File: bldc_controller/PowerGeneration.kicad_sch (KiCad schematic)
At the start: 67 parts, among them U2 MAX15062BATA+T, U3 ADP5301ACBZ-4-R7, U4 LP2992IM5-3.3/NOPB

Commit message: some progress on the pcb
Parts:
- removed NT2: GND_STAR, NetTie:NetTie-2_SMD_Pad2.0mm, symbol Device:NetTie_2
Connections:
- net +VBAT: no longer C?.2, C?.2, C?.2, C?.2, C?.2, C?.2, C?.2, C?.2, C?.2, C?.2, C?.2, C?.2, C?.2, C?.2, C?.2, C?.2
- net -VBAT: now also C?.2, C?.2, C?.2, C?.2, C?.2, C?.2, C?.2, C?.2, C?.2, C?.2, C?.2, C?.2, C?.2, C?.2, C?.2, C?.2
- net VID_3V3: now reaches U3.C3 (VID)
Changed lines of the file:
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@@
   )
   (no_connect (at 105.41 40.64))
-  (no_connect (at 217.17 45.72))
-  (no_connect (at 240.03 45.72))
+  (no_connect (at 208.28 45.72))
+  (no_connect (at 248.92 45.72))
   (wire (pts (xy 111.76 140.97) (xy 111.76 139.7))
     (stroke (width 0.381) (type default) (color 200 50 50 1))
@@
     (stroke (width 0.381) (type default) (color 0 0 0 1))
   )
+  (wire (pts (xy 248.92 45.72) (xy 240.03 45.72))
+    (stroke (width 0) (type default))
+  )
   (wire (pts (xy 27.94 139.7) (xy 31.75 139.7))
     (stroke (width 0.381) (type default) (color 200 50 50 1))
@@
     (stroke (width 0) (type default))
   )
-  (wire (pts (xy 229.87 142.24) (xy 233.68 142.24))
-    (stroke (width 0) (type default))
-  )
   (wire (pts (xy 217.17 33.02) (xy 215.9 33.02))
     (stroke (width 0) (type default))
@@
     (stroke (width 0) (type default))
   )
+  (wire (pts (xy 208.28 45.72) (xy 217.17 45.72))
+    (stroke (width 0) (type default))
+  )
   (wire (pts (xy 58.42 148.59) (xy 58.42 149.86))
     (stroke (width 0.381) (type default) (color 0 0 0 1))
@@
     (stroke (width 0.381) (type default) (color 0 0 0 1))
   )
-  (polyline (pts (xy 274.32 161.29) (xy 181.61 161.29))
-    (stroke (width 0) (type default))
-  )
   (wire (pts (xy 102.87 154.94) (xy 102.87 156.21))
     (stroke (width 0.381) (type default) (color 200 50 50 1))
@@
     (stroke (width 0.381) (type default) (color 200 50 50 1))
   )
-  (wire (pts (xy 217.17 146.05) (xy 219.71 146.05))
-    (stroke (width 0.381) (type default) (color 0 0 0 1))
-  )
   (wire (pts (xy 255.27 92.71) (xy 238.76 92.71))
     (stroke (width 0) (type default))
@@
     (stroke (width 0.381) (type default) (color 0 0 0 1))
   )
-  (wire (pts (xy 233.68 142.24) (xy 233.68 144.78))
-    (stroke (width 0) (type default))
-  )
   (wire (pts (xy 40.64 154.94) (xy 40.64 156.21))
     (stroke (width 0.381) (type default) (color 200 50 50 1))
@@
     (stroke (width 0) (type default))
   )
-  (polyline (pts (xy 177.8 138.43) (xy 177.8 157.48))
-    (stroke (width 0) (type default))
-  )
   (wire (pts (xy 93.98 170.18) (xy 102.87 170.18))
     (stroke (width 0.381) (type default) (color 200 50 50 1))
@@
     (stroke (width 0.381) (type default) (color 200 50 50 1))
   )
-  (polyline (pts (xy 278.13 138.43) (xy 278.13 157.48))
-    (stroke (width 0) (type default))
-  )
   (wire (pts (xy 35.56 54.61) (xy 30.48 54.61))
     (stroke (width 0.381) (type default) (color 0 0 0 1))
@@
     (stroke (width 0) (type default))
   )
-  (wire (pts (xy 219.71 142.24) (xy 219.71 146.05))
-    (stroke (width 0.381) (type default) (color 0 0 0 1))
-  )
   (wire (pts (xy 102.87 170.18) (xy 102.87 171.45))
     (stroke (width 0.381) (type default) (color 200 50 50 1))
@@
     (stroke (width 0) (type default))
   )
-  (wire (pts (xy 224.79 142.24) (xy 219.71 142.24))
-    (stroke (width 0.381) (type default) (color 0 0 0 1))
-  )
-  (polyline (pts (xy 181.61 134.62) (xy 274.32 134.62))
-    (stroke (width 0) (type default))
-  )
   (wire (pts (xy 255.27 86.36) (xy 257.81 86.36))
     (stroke (width 0) (type default))
@@
     (stroke (width 0.381) (type default) (color 0 0 0 1))
   )
-  (arc (start 278.12 157.47) (mid 277.007 160.167) (end 274.31 161.28)
+  (arc (start 21.59 193.04) (mid 18.893 191.927) (end 17.78 189.23)
     (stroke (width 0) (type default))
     (fill (type none))
   )
-  (arc (start 21.59 193.04) (mid 18.893 191.927) (end 17.78 189.23)
+  (arc (start 17.78 21.59) (mid 18.8959 18.8959) (end 21.59 17.78)
     (stroke (width 0) (type default))
     (fill (type none))
   )
-  (arc (start 17.78 21.59) (mid 18.8959 18.8959) (end 21.59 17.78)
+  (arc (start 278.13 125.73) (mid 277.0141 128.4241) (end 274.32 129.54)
     (stroke (width 0) (type default))
     (fill (type none))
   )
-  (arc (start 278.13 125.73) (mid 277.0141 128.4241) (end 274.32 129.54)
+  (arc (start 170.18 134.62) (mid 172.8773 135.7342) (end 173.99 138.43)
     (stroke (width 0) (type default))
     (fill (type none))
   )
-  (arc (start 170.18 134.62) (mid 172.8773 135.7342) (end 173.99 138.43)
+  (arc (start 17.78 138.43) (mid 18.8959 135.7359) (end 21.59 134.62)
     (stroke (width 0) (type default))
     (fill (type none))
   )
-  (arc (start 17.78 138.43) (mid 18.8959 135.7359) (end 21.59 134.62)
+  (arc (start 21.59 129.54) (mid 18.8959 128.4241) (end 17.78 125.73)
     (stroke (width 0) (type default))
     (fill (type none))
   )
-  (arc (start 177.81 138.44) (mid 178.923 135.743) (end 181.62 134.63)
+  (arc (start 274.32 17.78) (mid 277.0141 18.8959) (end 278.13 21.59)
     (stroke (width 0) (type default))
     (fill (type none))
   )
-  (arc (start 21.59 129.54) (mid 18.8959 128.4241) (end 17.78 125.73)
+  (arc (start 173.99 189.23) (mid 172.8741 191.9241) (end 170.18 193.04)
     (stroke (width 0) (type default))
     (fill (type none))
   )
-  (arc (start 274.31 134.63) (mid 277.007 135.743) (end 278.12 138.44)
-    (stroke (width 0) (type default))
-    (fill (type none))
-  )
-  (arc (start 274.32 17.78) (mid 277.0141 18.8959) (end 278.13 21.59)
-    (stroke (width 0) (type default))
-    (fill (type none))
-  )
-  (arc (start 173.99 189.23) (mid 172.8741 191.9241) (end 170.18 193.04)
-    (stroke (width 0) (type default))
-    (fill (type none))
-  )
   (arc (start 19.05 -215.9) (mid 21.6538 -222.1862) (end 27.94 -224.79)
-    (stroke (width 0) (type default))
-    (fill (type none))
-  )
-  (arc (start 181.62 161.28) (mid 178.923 160.167) (end 177.81 157.47)
     (stroke (width 0) (type default))
     (fill (type none))
@@
     (effects (font (size 1.524 1.524) (color 0 0 0 1)) (justify left top))
   )
-  (text_box "Ground star connection point"
-    (at 179.07 149.86 0) (size 97.79 9.525)
-    (stroke (width -0.0001) (type default))
-    (fill (type none))
-    (effects (font (size 2.54 2.54) (thickness 0.508) bold (color 0 0 0 1)) (justify bottom))
-  )
   (label "FB_3V3" (at 240.03 38.1 0) (fields_autoplaced)
     (effects (font (size 1.27 1.27)) (justify left bottom))
@@
     (effects (font (size 1.27 1.27)) (justify right bottom))
   )
-  (label "PG_3V3" (at 240.03 45.72 0) (fields_autoplaced)
-    (effects (font (size 1.27 1.27)) (justify left bottom))
+  (label "PG_3V3" (at 248.92 45.72 180) (fields_autoplaced)
+    (effects (font (size 1.27 1.27)) (justify right bottom))
   )
   (label "~{RST}_5V" (at 105.41 40.64 0) (fields_autoplaced)
@@
     (effects (font (size 1.27 1.27)) (justify left bottom))
   )
+  (label "VID_3V3" (at 209.55 45.72 0) (fields_autoplaced)
+    (effects (font (size 1.27 1.27)) (justify left bottom))
+  )
   (label "SW_3V3" (at 240.03 30.48 0) (fields_autoplaced)
     (effects (font (size 1.27 1.27)) (justify left bottom))
@@
     (effects (font (size 1.27 1.27) bold) (justify right))
   )
-  (hierarchical_label "-VBAT" (shape output) (at 217.17 146.05 180) (fields_autoplaced)
-    (effects (font (size 1.27 1.27) bold) (justify right))
-  )
   (hierarchical_label "-VBAT" (shape output) (at 27.94 149.86 180) (fields_autoplaced)
     (effects (font (size 1.27 1.27) bold) (justify right))
@@
     (effects (font (size 1.27 1.27) bold) (justify right))
   )
-  (hierarchical_label "+VBAT" (shape input) (at 27.94 180.34 180) (fields_autoplaced)
-    (effects (font (size 1.27 1.27) bold) (justify right))
-  )
   (hierarchical_label "-VBAT" (shape output) (at 27.94 165.1 180) (fields_autoplaced)
     (effects (font (size 1.27 1.27) bold) (justify right))
@@
   )
   (hierarchical_label "+VBAT" (shape input) (at 27.94 170.18 180) (fields_autoplaced)
+    (effects (font (size 1.27 1.27) bold) (justify right))
+  )
+  (hierarchical_label "-VBAT" (shape output) (at 27.94 180.34 180) (fields_autoplaced)
     (effects (font (size 1.27 1.27) bold) (justify right))
   )
@@
         (path "/0650c7a8-acba-429c-9f8e-eec0baf0bc1c/b89a7d22-bda3-4776-b5ce-8f6b0eb8f2a5"
           (reference "C8") (unit 1)
-        )
-      )
-    )
-  )
-  (symbol (lib_id "Device:NetTie_2") (at 227.33 142.24 180) (unit 1)
-    (in_bom no) (on_board yes) (dnp no)
-    (property "Reference" "NT2" (at 227.33 138.43 0)
-      (effects (font (size 1.27 1.27)))
-    )
-    (property "Value" "GND_STAR" (at 227.33 140.97 0)
-      (effects (font (size 1.27 1.27)))
-    )
-    (property "Footprint" "NetTie:NetTie-2_SMD_Pad2.0mm" (at 227.33 142.24 0)
-      (effects (font (size 1.27 1.27)) hide)
-    )
-    (property "Datasheet" "~" (at 227.33 142.24 0)
-      (effects (font (size 1.27 1.27)) hide)
-    )
-    (pin "1")
-    (pin "2")
-    (instances
-      (project "bldc_controller"
-        (path "/0650c7a8-acba-429c-9f8e-eec0baf0bc1c/b89a7d22-bda3-4776-b5ce-8f6b0eb8f2a5"
-          (reference "NT2") (unit 1)
         )
       )
@@
         )
       )
-    )
-  )
-  (symbol (lib_id "power:GND") (at 233.68 144.78 0) (unit 1)
-    (in_bom yes) (on_board yes) (dnp no) (fields_autoplaced)
-    (property "Reference" "#PWR010" (at 233.68 151.13 0)
-      (effects (font (size 1.27 1.27)) hide)
-    )
-    (property "Value" "GND" (at 233.68 149.86 0)
-      (effects (font (size 1.27 1.27)))
-    )
-    (property "Footprint" "" (at 233.68 144.78 0)
-      (effects (font (size 1.27 1.27)) hide)
-    )
-    (property "Datasheet" "" (at 233.68 144.78 0)
-      (effects (font (size 1.27 1.27)) hide)
-    )
-    (pin "1")
-    (instances
-      (project "bldc_controller"
-        (path "/0650c7a8-acba-429c-9f8e-eec0baf0bc1c/b89a7d22-bda3-4776-b5ce-8f6b0eb8f2a5"
-          (reference "#PWR010") (unit 1)
-        )
-      )

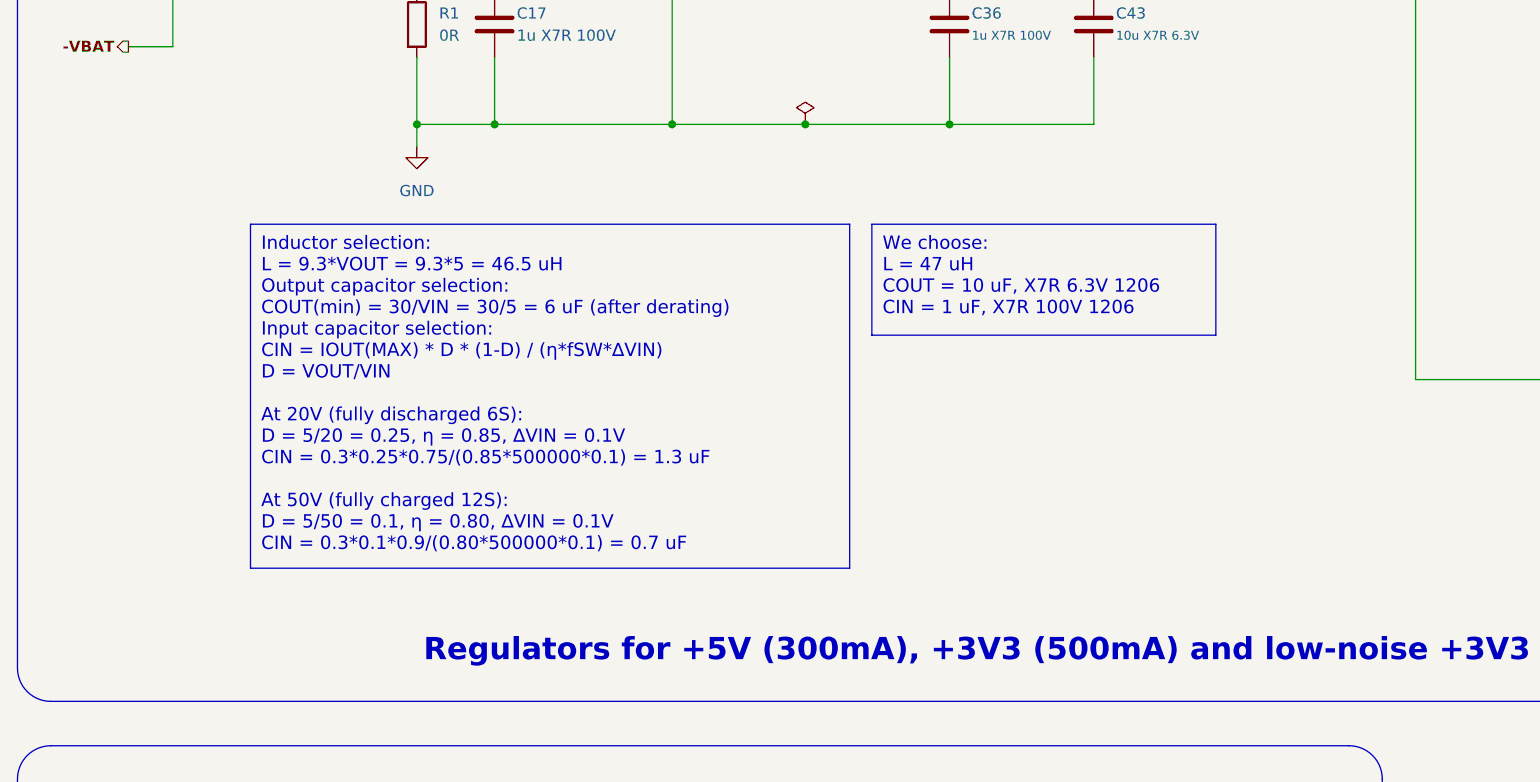
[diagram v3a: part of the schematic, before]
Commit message: added 12V buck
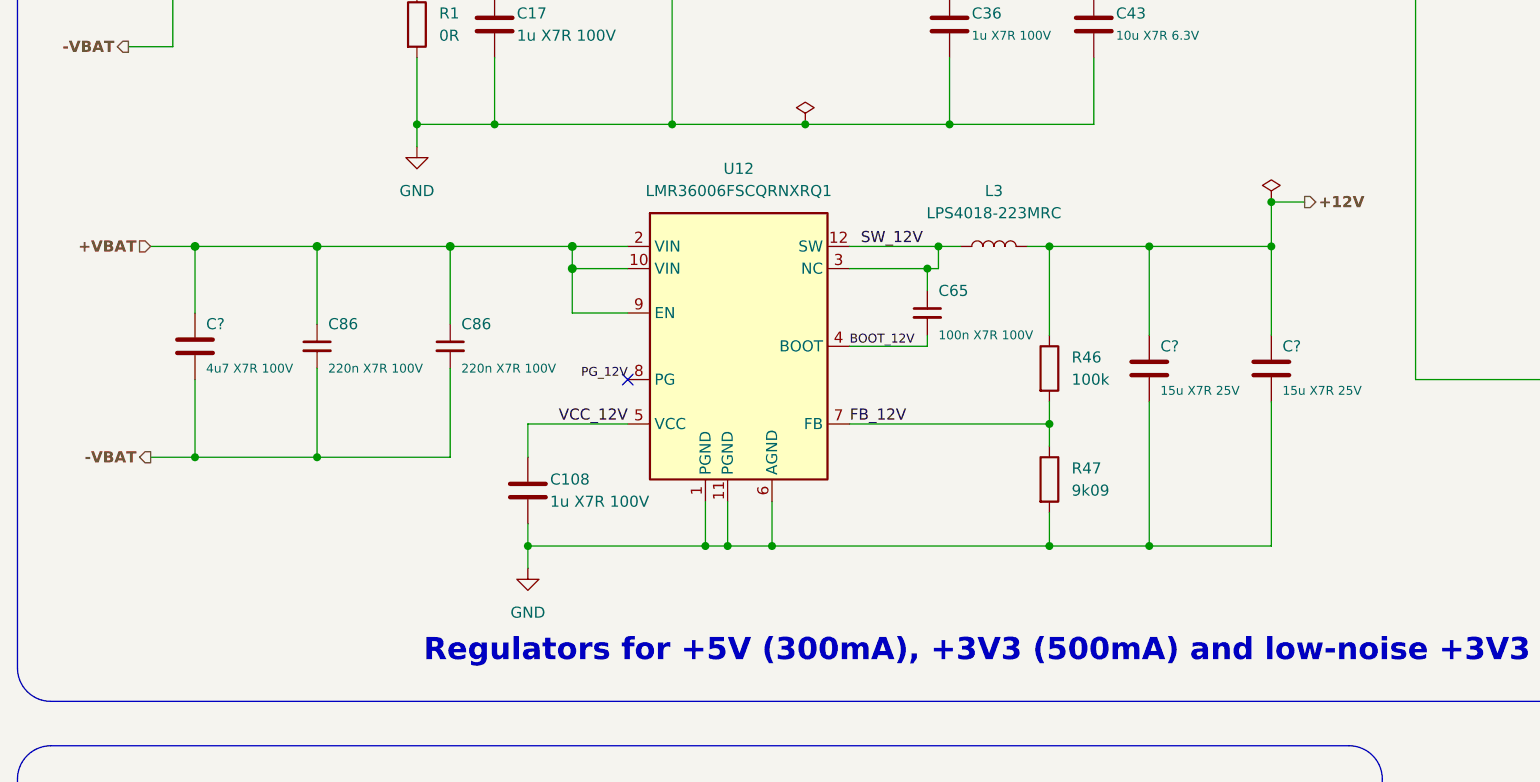
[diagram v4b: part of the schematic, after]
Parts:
- added C108: 1u X7R 100V, 0_capacitor_smd:C_0402_1005_DensityHigh, symbol Device:C
- added C65: 100n X7R 100V, 0_capacitor_smd:C_0402_1005_DensityHigh, symbol Device:C_Small
- added C86 (x2): 220n X7R 100V, 0_capacitor_smd:C_0402_1005_DensityHigh, symbol Device:C_Small
- added C?: 4u7 X7R 100V, 0_capacitor_smd:C_1206_3216_DensityHigh, symbol Device:C
- added C? (x2): 15u X7R 25V, 0_capacitor_smd:C_1210_3225_DensityHigh, symbol Device:C
- added L3: LPS4018-223MRC, Inductor_SMD:L_Coilcraft_LPS4018, symbol Device:L
- added R46: 100k, 0_resistor_smd:R_0402_1005_DensityHigh, symbol Device:R
- added R47: 9k09, 0_resistor_smd:R_0402_1005_DensityHigh, symbol Device:R
- added U12: LMR36006FSCQRNXRQ1, 0_switching_regulator:LMR36006FSCQRNXRQ1, symbol 0_switching_regulator:LMR36006FSCQRNXRQ1
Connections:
- net +VBAT: now also C86.1, C86.1, C?.1, U12.10 (VIN), U12.2 (VIN), U12.9 (EN)
- net -VBAT: now also C86.2, C86.2, C?.2
- net GND: now also C108.2, C?.2, C?.2, R47.2, U12.1 (PGND), U12.11 (PGND), U12.6 (AGND)
- new net +12V: C?.1, C?.1, L3.2, R46.1
- new net BOOT_12V: C65.2, U12.4 (BOOT)
- new net FB_12V: R46.2, R47.1, U12.7 (FB)
- new net PG_12V: U12.8 (PG)
- new net SW_12V: C65.1, L3.1, U12.12 (SW), U12.3 (NC)
- new net VCC_12V: C108.1, U12.5 (VCC)
- no-connect marks 3 -> 4

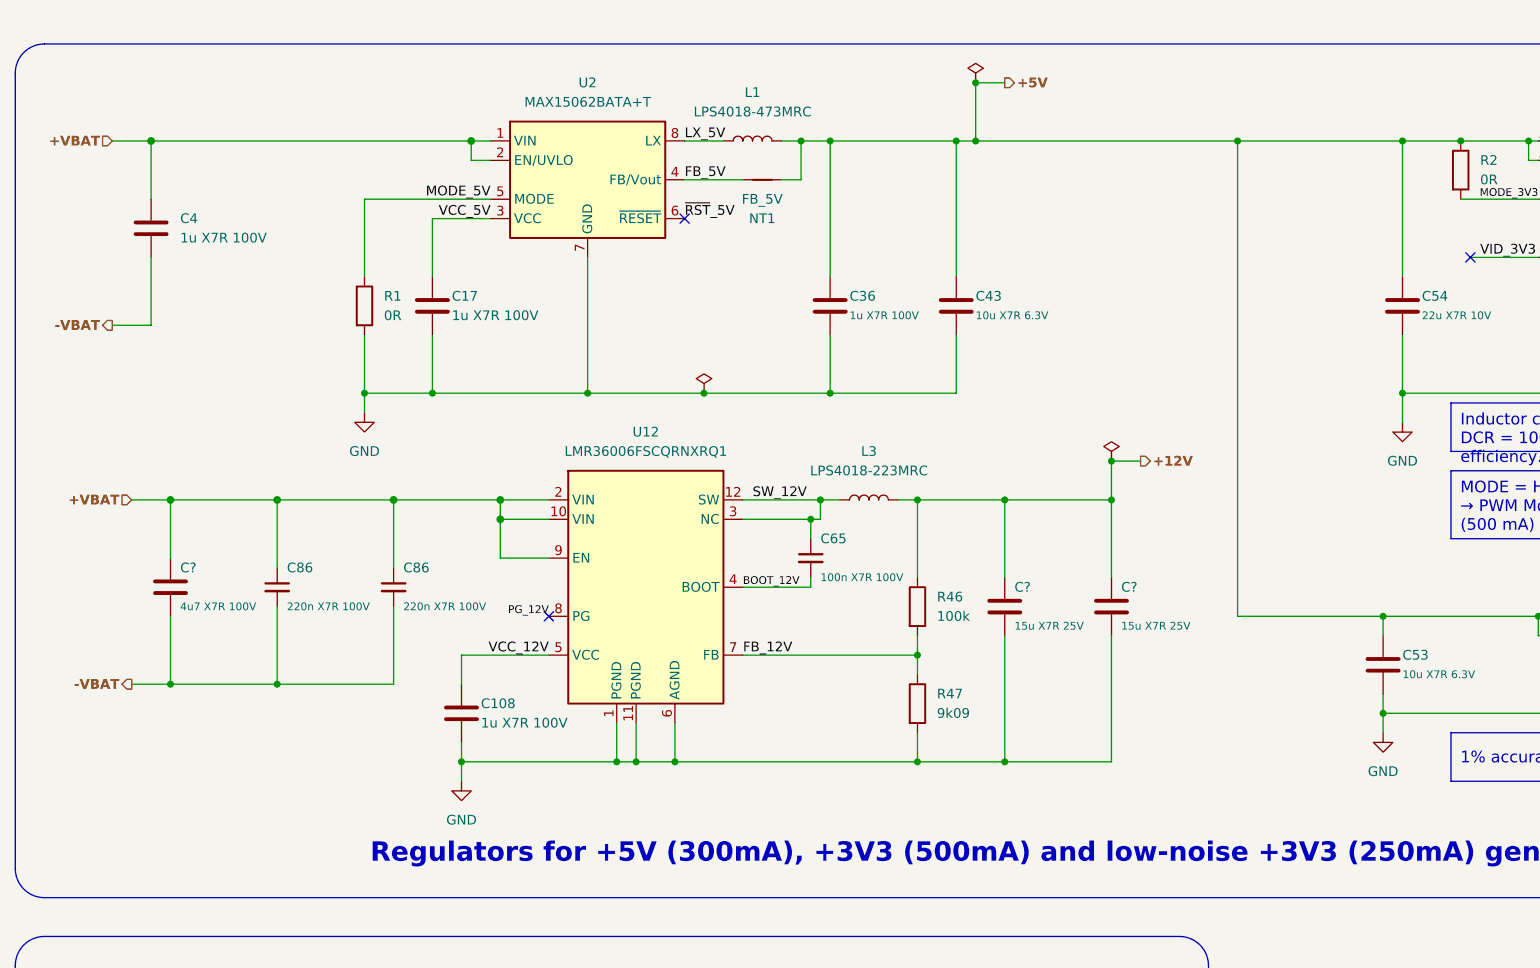
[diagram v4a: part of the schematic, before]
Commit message: routed 12V buck. Need to change mcu package and add fan low-side switch
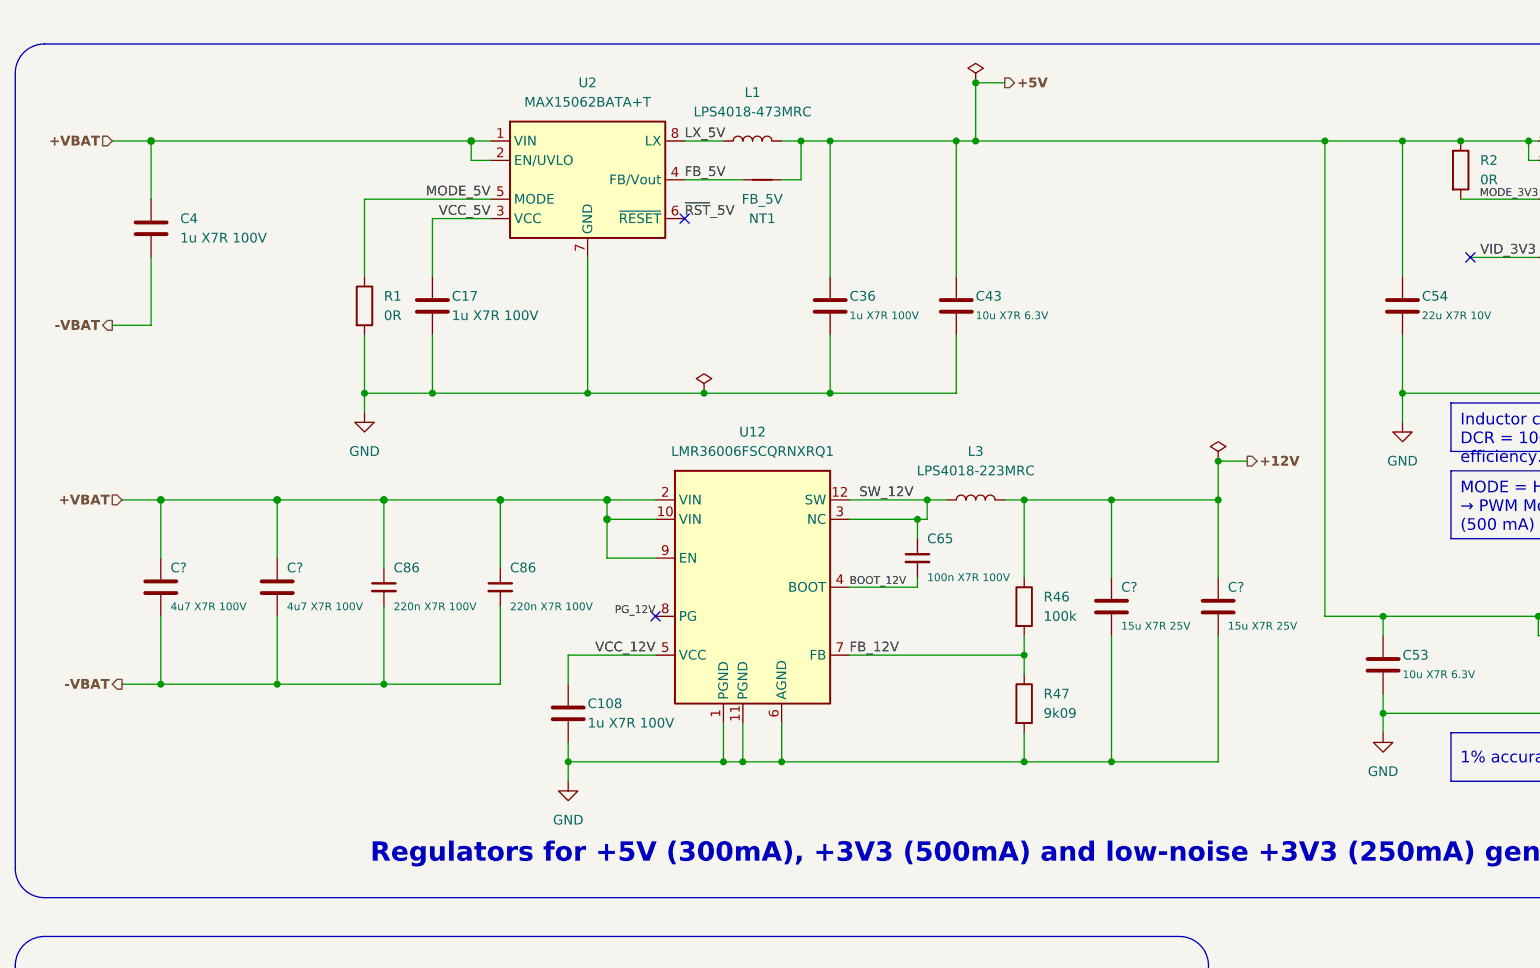
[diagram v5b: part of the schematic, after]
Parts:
- added C?: 4u7 X7R 100V, 0_capacitor_smd:C_1206_3216_DensityHigh, symbol Device:C
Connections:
- net +VBAT: now also C?.1
- net -VBAT: now also C?.2
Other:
- moved on the sheet: C108, C65, C86, C?, L3, R46, R47, U12
